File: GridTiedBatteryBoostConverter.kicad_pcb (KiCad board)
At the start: 2 copper layers, 270.1 x 143.1 mm, 161 parts, among them J101 Battery Connection, J103 Solar Panels, J202 Conn_01x03_Female, J203 I2C_BUS, J401 Screw_Terminal_01x02, J402 AudioJack2_SwitchT, Q101 IXFP36N20X3, Q102 BC847B-13-F, Q103 SSM3K329R, Q104 SSM3J334R, Q201 SSM3K329R, Q202 SSM3K329R, Q203 SSM3J334R, Q301 BC847B-13-F, Q302 BC856B-13-F, Q305 IRFP4321PBF, Q306 IRFP4321PBF, SW201 SW_Up, SW202 SW_Down, SW203 SW_Enter, U101 OPA2837IDGKR, U102 UCC2800DTR, U201 LCD 2004A Right Angle Header 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, U202 Teensy-LC, U203 PCF8574ADWR, U204 ESP-WROOM-02U, U301 FDA217, U302 LTC7138EMSE-PBF, U303 TPS560200DBVR, U304 TLV70430DBVT, U305 REF2925AIDBZT, U306 TPS560200DBVR

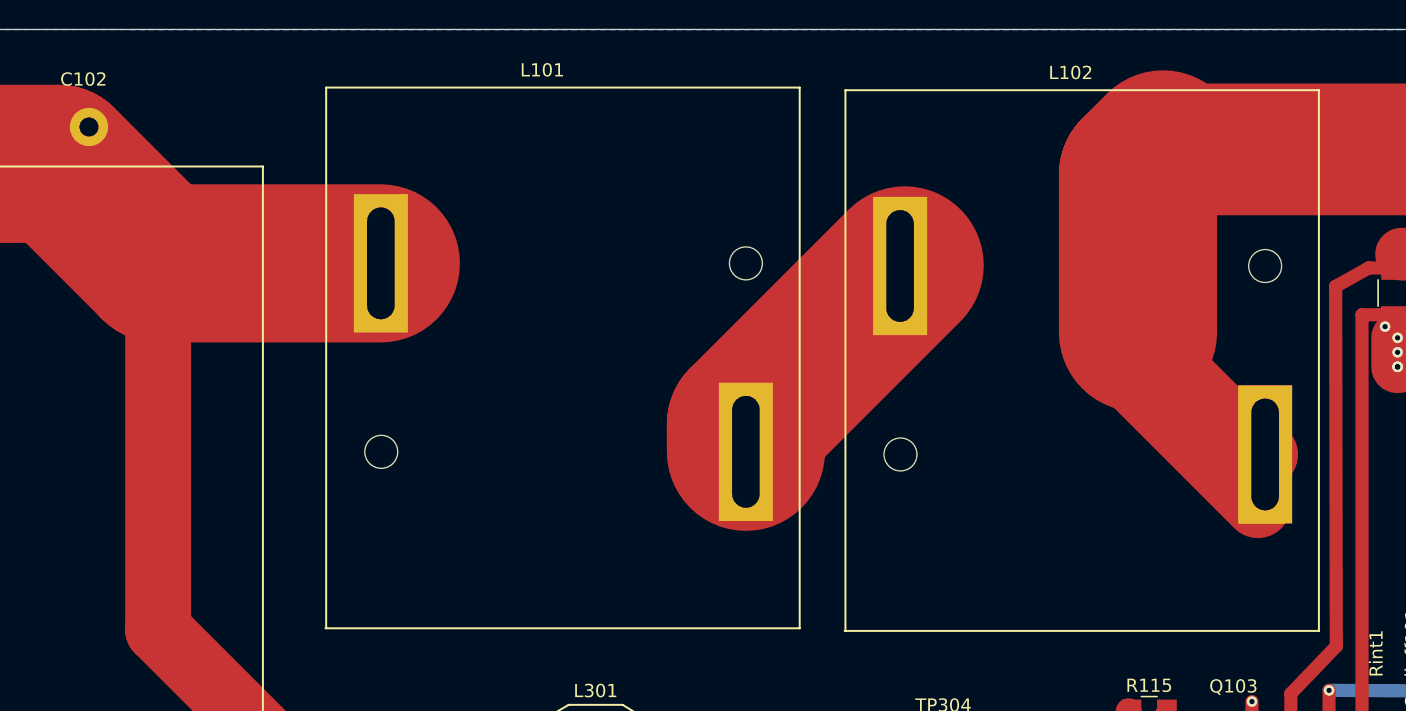
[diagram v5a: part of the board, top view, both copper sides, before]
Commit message: The Wurth main inductors turned up today, and I spotted a stuff up with the footprint layout, pins are in the right spot, but the body outline is  x-y switched, so the 2 inductors would not fit, so fix was to just rotate them and reroute.
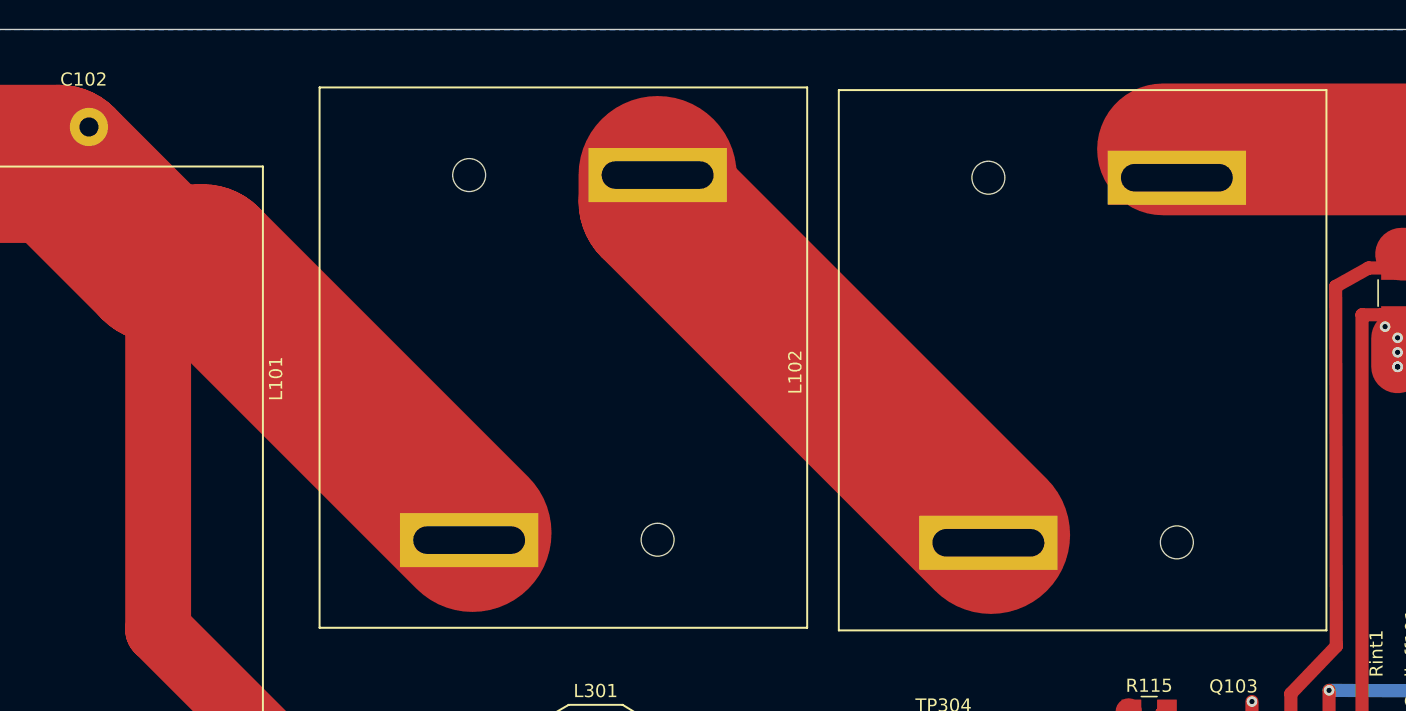
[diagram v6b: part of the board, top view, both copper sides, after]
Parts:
- turned L101 to 180 degrees
- turned L102 to 180 degrees
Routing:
- net Net-(D101-Pad2): track 101.4 -> 54.2 mm
- net Net-(L101-Pad1): track 19.1 -> 37.8 mm
- net Vin: track 211.1 -> 226.5 mm
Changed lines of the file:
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@@
     (thickness 1.6)
     (drawings 39)
-    (tracks 1122)
+    (tracks 1113)
     (zones 0)
     (modules 161)
@@
   )
   (setup
-    (last_trace_width 1)
+    (last_trace_width 12)
     (user_trace_width 0.5)
     (user_trace_width 1)
@@
     (add_net "Net-(F101-Pad1)")
   )
+  (module Inductors_jl:Inductor_Wurth_7443763540470 (layer F.Cu)
+    (at 119.5 39.4 180)
+    (fp_text reference L101 (at 21.8 -1.6 270) (layer F.SilkS)
+      (effects (font (size 1 1) (thickness 0.15)))
+    )
+    (fp_text value "47uH 31A Sat 6.38m Ohm" (at 23.5 -0.9 270) (layer F.Fab)
+      (effects (font (size 1 1) (thickness 0.15)))
+    )
+    (fp_line (start -18.5 20.5) (end -18.5 -20.5) (layer F.SilkS) (width 0.15))
+    (fp_line (start 18.5 20.5) (end -18.5 20.5) (layer F.SilkS) (width 0.15))
+    (fp_line (start 18.5 -20.5) (end 18.5 20.5) (layer F.SilkS) (width 0.15))
+    (fp_line (start -18.5 -20.5) (end 18.5 -20.5) (layer F.SilkS) (width 0.15))
+    (pad 1 thru_hole rect (at -7.15 13.85 180) (size 10.5 4.1) (drill oval 8.5 2.1) (layers *.Cu *.Mask)
+      (net 31 "Net-(L101-Pad1)"))
+    (pad 2 thru_hole rect (at 7.15 -13.85 180) (size 10.5 4.1) (drill oval 8.5 2.1) (layers *.Cu *.Mask)
+      (net 2 Vin))
+    (pad "" np_thru_hole circle (at 7.15 13.85 180) (size 2.5 2.5) (drill 2.5) (layers *.Cu *.Mask))
+    (pad "" np_thru_hole circle (at -7.15 -13.82 180) (size 2.5 2.5) (drill 2.5) (layers *.Cu *.Mask))
+  )
+  (module Inductors_jl:Inductor_Wurth_7443763540470 (layer F.Cu)
+    (at 158.9 39.6 180)
+    (fp_text reference L102 (at 21.8 -0.9 270) (layer F.SilkS)
+      (effects (font (size 1 1) (thickness 0.15)))
+    )
+    (fp_text value "47uH 31A Sat 6.38m Ohm" (at 23.6 -0.4 270) (layer F.Fab)
+      (effects (font (size 1 1) (thickness 0.15)))
+    )
+    (fp_line (start -18.5 20.5) (end -18.5 -20.5) (layer F.SilkS) (width 0.15))
+    (fp_line (start 18.5 20.5) (end -18.5 20.5) (layer F.SilkS) (width 0.15))
+    (fp_line (start 18.5 -20.5) (end 18.5 20.5) (layer F.SilkS) (width 0.15))
+    (fp_line (start -18.5 -20.5) (end 18.5 -20.5) (layer F.SilkS) (width 0.15))
+    (pad 1 thru_hole rect (at -7.15 13.85 180) (size 10.5 4.1) (drill oval 8.5 2.1) (layers *.Cu *.Mask)
+      (net 24 "Net-(D101-Pad2)"))
+    (pad 2 thru_hole rect (at 7.15 -13.85 180) (size 10.5 4.1) (drill oval 8.5 2.1) (layers *.Cu *.Mask)
+      (net 31 "Net-(L101-Pad1)"))
+    (pad "" np_thru_hole circle (at 7.15 13.85 180) (size 2.5 2.5) (drill 2.5) (layers *.Cu *.Mask))
+    (pad "" np_thru_hole circle (at -7.15 -13.82 180) (size 2.5 2.5) (drill 2.5) (layers *.Cu *.Mask))
+  )
   (module Transformers_ThroughHole_jl:FS10-110-C2 (layer F.Cu)
     (at 260.95 142.35 90)
@@
   (module teensy:Teensy30_31_32_LC (layer F.Cu)
     (at 165.6 113.6)
+    (clearance 0.5)
     (fp_text reference U202 (at 11.3 -11.1) (layer F.SilkS)
       (effects (font (size 1 1) (thickness 0.15)))
@@
     (pad "" np_thru_hole circle (at 0 -3.5 180) (size 1.3 1.3) (drill 1.3) (layers *.Cu *.Mask))
   )
-  (module Inductors_jl:Inductor_Wurth_7443763540470 (layer F.Cu)
-    (at 119.5 39.4 90)
-    (fp_text reference L101 (at 21.8 -1.6 180) (layer F.SilkS)
-      (effects (font (size 1 1) (thickness 0.15)))
-    )
-    (fp_text value "47uH 31A Sat 6.38m Ohm" (at 23.5 -0.9 180) (layer F.Fab)
-      (effects (font (size 1 1) (thickness 0.15)))
-    )
-    (fp_line (start -20.54 -18) (end 20.49 -18) (layer F.SilkS) (width 0.15))
-    (fp_line (start 20.49 -18) (end 20.49 17.93) (layer F.SilkS) (width 0.15))
-    (fp_line (start 20.49 17.93) (end -20.54 17.93) (layer F.SilkS) (width 0.15))
-    (fp_line (start -20.54 17.93) (end -20.54 -18.06) (layer F.SilkS) (width 0.15))
-    (pad 1 thru_hole rect (at -7.15 13.85 90) (size 10.5 4.1) (drill oval 8.5 2.1) (layers *.Cu *.Mask)
-      (net 31 "Net-(L101-Pad1)"))
-    (pad 2 thru_hole rect (at 7.15 -13.85 90) (size 10.5 4.1) (drill oval 8.5 2.1) (layers *.Cu *.Mask)
-      (net 2 Vin))
-    (pad "" np_thru_hole circle (at 7.15 13.85 90) (size 2.5 2.5) (drill 2.5) (layers *.Cu *.Mask))
-    (pad "" np_thru_hole circle (at -7.15 -13.82 90) (size 2.5 2.5) (drill 2.5) (layers *.Cu *.Mask))
-  )
-  (module Inductors_jl:Inductor_Wurth_7443763540470 (layer F.Cu)
-    (at 158.9 39.6 90)
-    (fp_text reference L102 (at 21.8 -0.9 180) (layer F.SilkS)
-      (effects (font (size 1 1) (thickness 0.15)))
-    )
-    (fp_text value "47uH 31A Sat 6.38m Ohm" (at 23.6 -0.4 180) (layer F.Fab)
-      (effects (font (size 1 1) (thickness 0.15)))
-    )
-    (fp_line (start -20.54 -18) (end 20.49 -18) (layer F.SilkS) (width 0.15))
-    (fp_line (start 20.49 -18) (end 20.49 17.93) (layer F.SilkS) (width 0.15))
-    (fp_line (start 20.49 17.93) (end -20.54 17.93) (layer F.SilkS) (width 0.15))
-    (fp_line (start -20.54 17.93) (end -20.54 -18.06) (layer F.SilkS) (width 0.15))
-    (pad 1 thru_hole rect (at -7.15 13.85 90) (size 10.5 4.1) (drill oval 8.5 2.1) (layers *.Cu *.Mask)
-      (net 24 "Net-(D101-Pad2)"))
-    (pad 2 thru_hole rect (at 7.15 -13.85 90) (size 10.5 4.1) (drill oval 8.5 2.1) (layers *.Cu *.Mask)
-      (net 31 "Net-(L101-Pad1)"))
-    (pad "" np_thru_hole circle (at 7.15 13.85 90) (size 2.5 2.5) (drill 2.5) (layers *.Cu *.Mask))
-    (pad "" np_thru_hole circle (at -7.15 -13.82 90) (size 2.5 2.5) (drill 2.5) (layers *.Cu *.Mask))
-  )
   (module Inductors_jl:Inductor_Bourns_PM3308 (layer F.Cu)
     (at 127.9 70.75 180)
@@
   (segment (start 81.2 24.7) (end 65.9 24.7) (width 12) (layer F.Cu) (net 2))
   (segment (start 88.75 32.25) (end 81.2 24.7) (width 12) (layer F.Cu) (net 2))
-  (segment (start 105.65 32.25) (end 88.75 32.25) (width 12) (layer F.Cu) (net 2))
   (segment (start 64.3 26.3) (end 65.9 24.7) (width 6) (layer F.Cu) (net 2))
   (segment (start 65.9 24.7) (end 68.6 22) (width 6) (layer F.Cu) (net 2))
-  (segment (start 105.65 32.25) (end 105.65 32.35) (width 1) (layer F.Cu) (net 2))
   (via (at 122.8 87.4) (size 0.8) (drill 0.4) (layers F.Cu B.Cu) (net 2))
   (segment (start 122.8 87.4) (end 122.8 91.1) (width 1) (layer B.Cu) (net 2))
@@
   (segment (start 122.74943 87.34943) (end 122.8 87.4) (width 0.5) (layer F.Cu) (net 2))
   (segment (start 121.1 87.34943) (end 122.74943 87.34943) (width 0.5) (layer F.Cu) (net 2))
+  (segment (start 88.75 32.25) (end 92.15 32.25) (width 12) (layer F.Cu) (net 2))
+  (segment (start 92.15 32.25) (end 112.6 52.7) (width 12) (layer F.Cu) (net 2))
   (via (at 53.65 131.25) (size 0.6) (drill 0.3) (layers F.Cu B.Cu) (net 3))
   (via (at 52.45 131.2) (size 0.6) (drill 0.3) (layers F.Cu B.Cu) (net 3))
@@
   (segment (start 191.75 72.2) (end 191.75 70.45) (width 1) (layer F.Cu) (net 23))
   (segment (start 191.75 70.45) (end 190.9 69.6) (width 1) (layer F.Cu) (net 23))
-  (segment (start 163.1 37.5) (end 163.1 25.5) (width 12) (layer F.Cu) (net 24))
-  (segment (start 163.1 25.5) (end 165 23.6) (width 12) (layer F.Cu) (net 24))
   (segment (start 165 23.6) (end 190.7 23.6) (width 10) (layer F.Cu) (net 24))
-  (segment (start 172.75 46.75) (end 172.35 46.75) (width 5) (layer F.Cu) (net 24))
-  (segment (start 163.85 38.25) (end 161.55 38.25) (width 5) (layer F.Cu) (net 24))
-  (segment (start 163.85 38.25) (end 163.1 37.5) (width 5) (layer F.Cu) (net 24))
-  (segment (start 172.35 46.75) (end 163.85 38.25) (width 5) (layer F.Cu) (net 24))
-  (segment (start 161.55 38.25) (end 162.5 39.2) (width 5) (layer F.Cu) (net 24))
-  (segment (start 162.5 39.2) (end 162.5 40.9) (width 5) (layer F.Cu) (net 24))
-  (segment (start 162.5 40.9) (end 172.2 50.6) (width 5) (layer F.Cu) (net 24))
   (segment (start 190.7 23.6) (end 199.5 23.6) (width 10) (layer F.Cu) (net 24))
   (segment (start 192.2 25.1) (end 190.7 23.6) (width 2) (layer F.Cu) (net 24))
@@
   (via (at 33.05 74.580002) (size 3.2) (drill 1.6) (layers F.Cu B.Cu) (net 30))
   (segment (start 33.05 67.35) (end 33.05 74.580002) (width 5) (layer B.Cu) (net 30))
+  (segment (start 126.65 25.55) (end 126.65 27.55) (width 12) (layer F.Cu) (net 31))
+  (segment (start 126.65 27.55) (end 151.95 52.85) (width 12) (layer F.Cu) (net 31))
   (segment (start 272.5746 118.1246) (end 272.6 118.15) (width 1) (layer F.Cu) (net 124))
-  (segment (start 133.35 46.55) (end 133.35 44.45) (width 12) (layer F.Cu) (net 31))
-  (segment (start 133.35 44.45) (end 145.4 32.4) (width 12) (layer F.Cu) (net 31))
   (segment (start 142.75 78.95) (end 142.75 77.45) (width 0.5) (layer F.Cu) (net 32))
   (segment (start 142.75 77.45) (end 143.6 76.6) (width 0.5) (layer F.Cu) (net 32))

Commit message: Found that my local updates of Kicad footprint librarys, had changed the names of resistor and capacitor footprints, so I updated all these footprint names.  Added circuit to measure the Vin via pin 28 of the Teensy-LC, This will allow the battery system to shut down if the battery voltage gets too low.
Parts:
- removed the REF*** at (267.6, 152.6)
- added D104: BAT54S, Package_TO_SOT_SMD:SOT-23_Handsoldering, F.Cu at (163.2, 89.1)
- added R121: 105k 0.1%, Resistor_SMD:R_0805_2012Metric_Pad1.15x1.40mm_HandSolder, F.Cu at (101.0, 79.9)
- added R122: 1.5K 0.1%, Resistor_SMD:R_0805_2012Metric_Pad1.15x1.40mm_HandSolder, F.Cu at (101.0, 84.2)
- C101: footprint Capacitors_ThroughHole:CP_Radial_D22.0mm_P10.00mm_SnapIn -> Capacitor_THT:CP_Radial_D22.0mm_P10.00mm_SnapIn
- C103: footprint Capacitors_ThroughHole:CP_Radial_D35.0mm_P10.00mm_SnapIn -> Capacitor_THT:CP_Radial_D35.0mm_P10.00mm_SnapIn
- C105, C106, C107, C108, C109, C110, C111, C112, C113, C114, C115, C201, C202, C203, C205, C302, C304, C309, C312, C313, C401, Cint101, Crolloff101, Ct101: footprint Capacitors_SMD:C_0805_HandSoldering -> Capacitor_SMD:C_0805_2012Metric_Pad1.15x1.40mm_HandSolder
- C204, C301, C305, C307, C308, C310, C311: footprint Capacitors_SMD:C_1206_HandSoldering -> Capacitor_SMD:C_1206_3216Metric_Pad1.42x1.75mm_HandSolder
- C303, C314: footprint Capacitors_SMD:C_2220_HandSoldering -> Capacitor_SMD:C_2220_5650Metric_Pad1.97x5.40mm_HandSolder
- C306, C315: footprint Capacitors_SMD:C_1812_HandSoldering -> Capacitor_SMD:C_1812_4532Metric_Pad1.30x3.40mm_HandSolder
- D301: footprint Diodes_SMD:D_SMA_Handsoldering -> Diode_SMD:D_SMA_Handsoldering
- R101, R102, R103, R104, R105, R106, R107, R108, R109, R110, R111, R112, R113, R115, R116, R117, R118, R119, R201, R202, R203, R204, R205, R206, R207, R208, R209, R210, R211, R212, R213, R301, R302, R303, R304, R308, R309, R310, R311, R312, R401, R402, R404, R405, R406, Rint1, Rint2, Rt101: footprint Resistors_SMD:R_0805_HandSoldering -> Resistor_SMD:R_0805_2012Metric_Pad1.15x1.40mm_HandSolder
- R114, R120: footprint Resistors_SMD:R_1210_HandSoldering -> Resistor_SMD:R_1210_3225Metric_Pad1.42x2.65mm_HandSolder
- moved C314 0.66 mm to (73.5, 94.6)
- moved R118 0.32 mm to (195.0, 87.5)
- moved R117 0.30 mm to (194.1, 90.8)
- moved R202 0.25 mm to (122.0, 141.7)
- moved R203 0.25 mm to (119.8, 139.6)
- moved C306 0.21 mm to (126.3, 81.8)
- moved Rt101 0.11 mm to (194.4, 69.7)
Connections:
- U202 pad 28: Net-(U202-Pad28) -> Battery_Voltage
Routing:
- net Battery_Voltage: track 0.00 -> 125.8 mm, vias 0 -> 4
- net /PowerSupplies/CHARGER_ON_OFF: track 104.2 -> 128.0 mm
- net +5V: track 420.4 -> 429.1 mm
- net 0: track 335.6 -> 344.1 mm, vias 88 -> 90
- net Vin: track 226.5 -> 233.2 mm
- net +3.0V: track 102.8 -> 106.1 mm
- net Net-(J103-Pad2): track 135.4 -> 136.0 mm

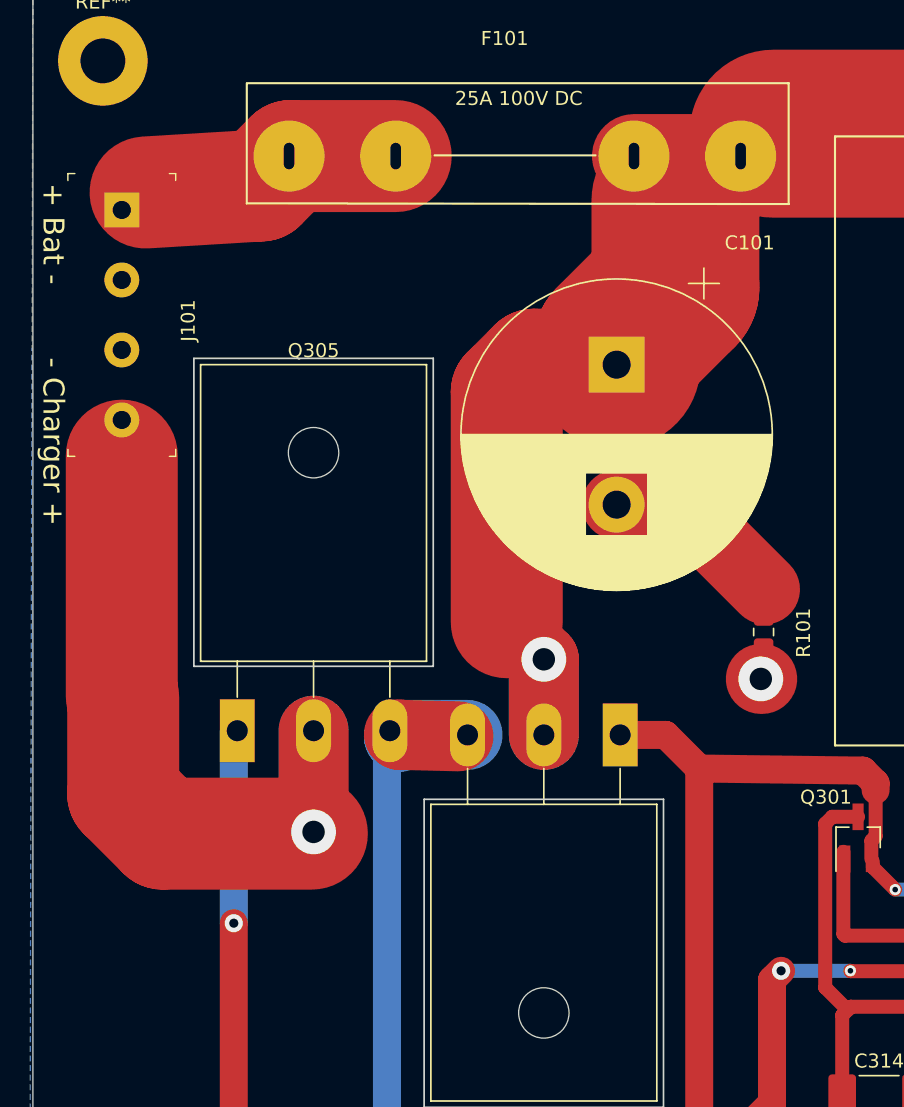
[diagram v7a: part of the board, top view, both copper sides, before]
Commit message: Added a dedicated fuse for the charger connection.  Lowered the fuses from 25A to 20A after looking more closely at the data sheet.  Charger is 19.5A atmost and Battery current draw at 80% efficency, 86.8V, 1000W is 14.4A. Reduced the voltage divider resistance for the MainPowerMonitor from 2x 10K to 2x 1K, the reason for this is to draw 1.25mA from the 3.0V supply to increase its effectiveness as input protection for the micro inputs, the BAT54S diodes connect to the 3.0V power supplys so will conduct to this if the input risees a diode drop above 3.0V, so the more current draw from this supply the more it can sink without rising.
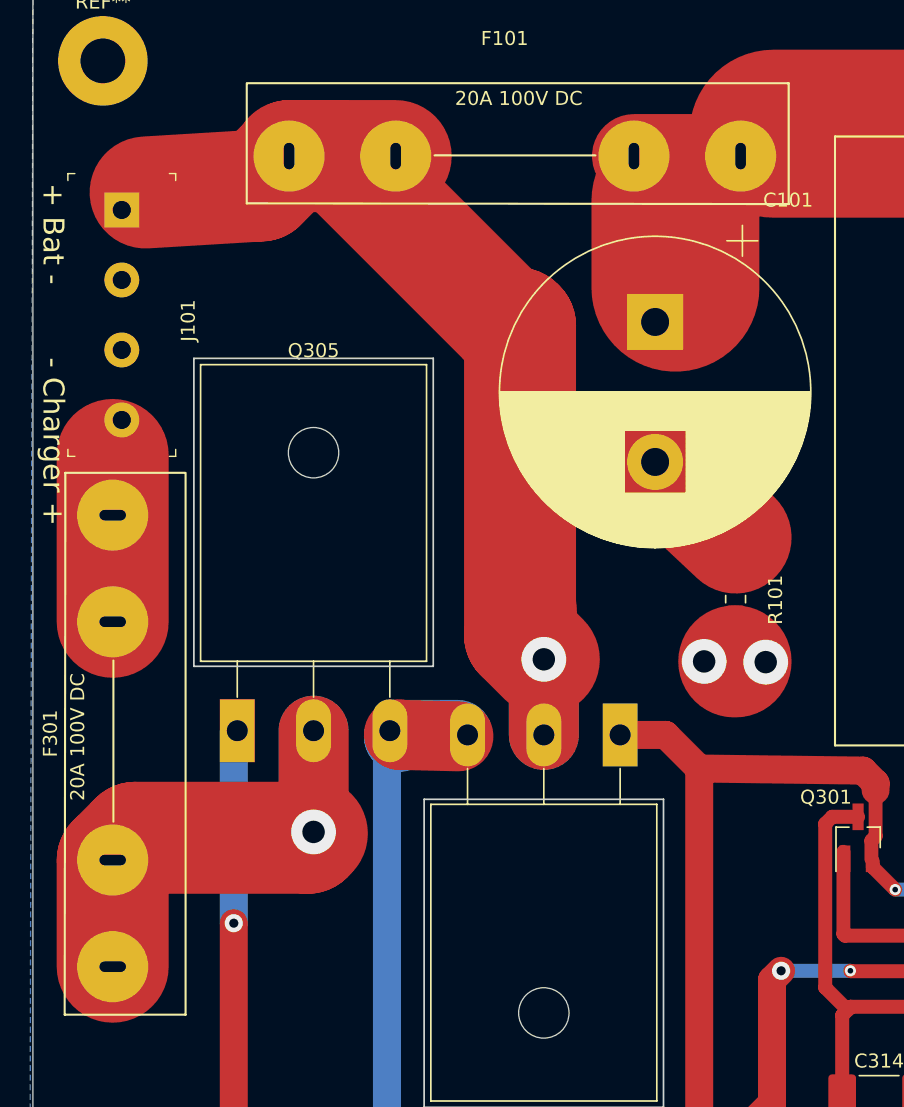
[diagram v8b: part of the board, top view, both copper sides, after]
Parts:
- added F301: Fuse Holder, Connect_jl:BellFuse_6.3mmX32mm_FC_102-22, F.Cu at (18.7, 52.0)
- R405, R406: value 10K 0.1% -> 1K 1%
- moved C101 4.11 mm to (57.5, 38.1)
- moved R101 3.09 mm to (63.2, 58.0)
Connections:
- F101 pad 1: Net-(F101-Pad1) -> ChargerVin
- J101 pad 1: Net-(F101-Pad1) -> ChargerVin
- Q305 pad 2: ChargerConnection -> Net-(F301-Pad2)
- Q306 pad 2: Vin -> ChargerVin
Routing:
- net ChargerVin: track 0.00 -> 79.6 mm, vias 0 -> 1
- net Vin: track 233.2 -> 181.1 mm, vias 3 -> 2
- net ChargerConnection: track 53.4 -> 11.9 mm, vias 1 -> 0
- net Net-(F301-Pad2): track 0.00 -> 37.3 mm, vias 0 -> 1
- net Net-(F101-Pad1): track 19.0 -> 0.00 mm
- net Net-(C101-Pad2): track 13.1 -> 7.89 mm
- net /PowerSupplies/Charger_FETs_Source: track 123.9 -> 123.2 mm
- net 0: vias 90 -> 91
